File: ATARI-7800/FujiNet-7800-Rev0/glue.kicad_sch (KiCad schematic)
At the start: 10 parts, among them U3 74HCT14, U4 74HCT00, U5 74HCT20, U6 74HCT20

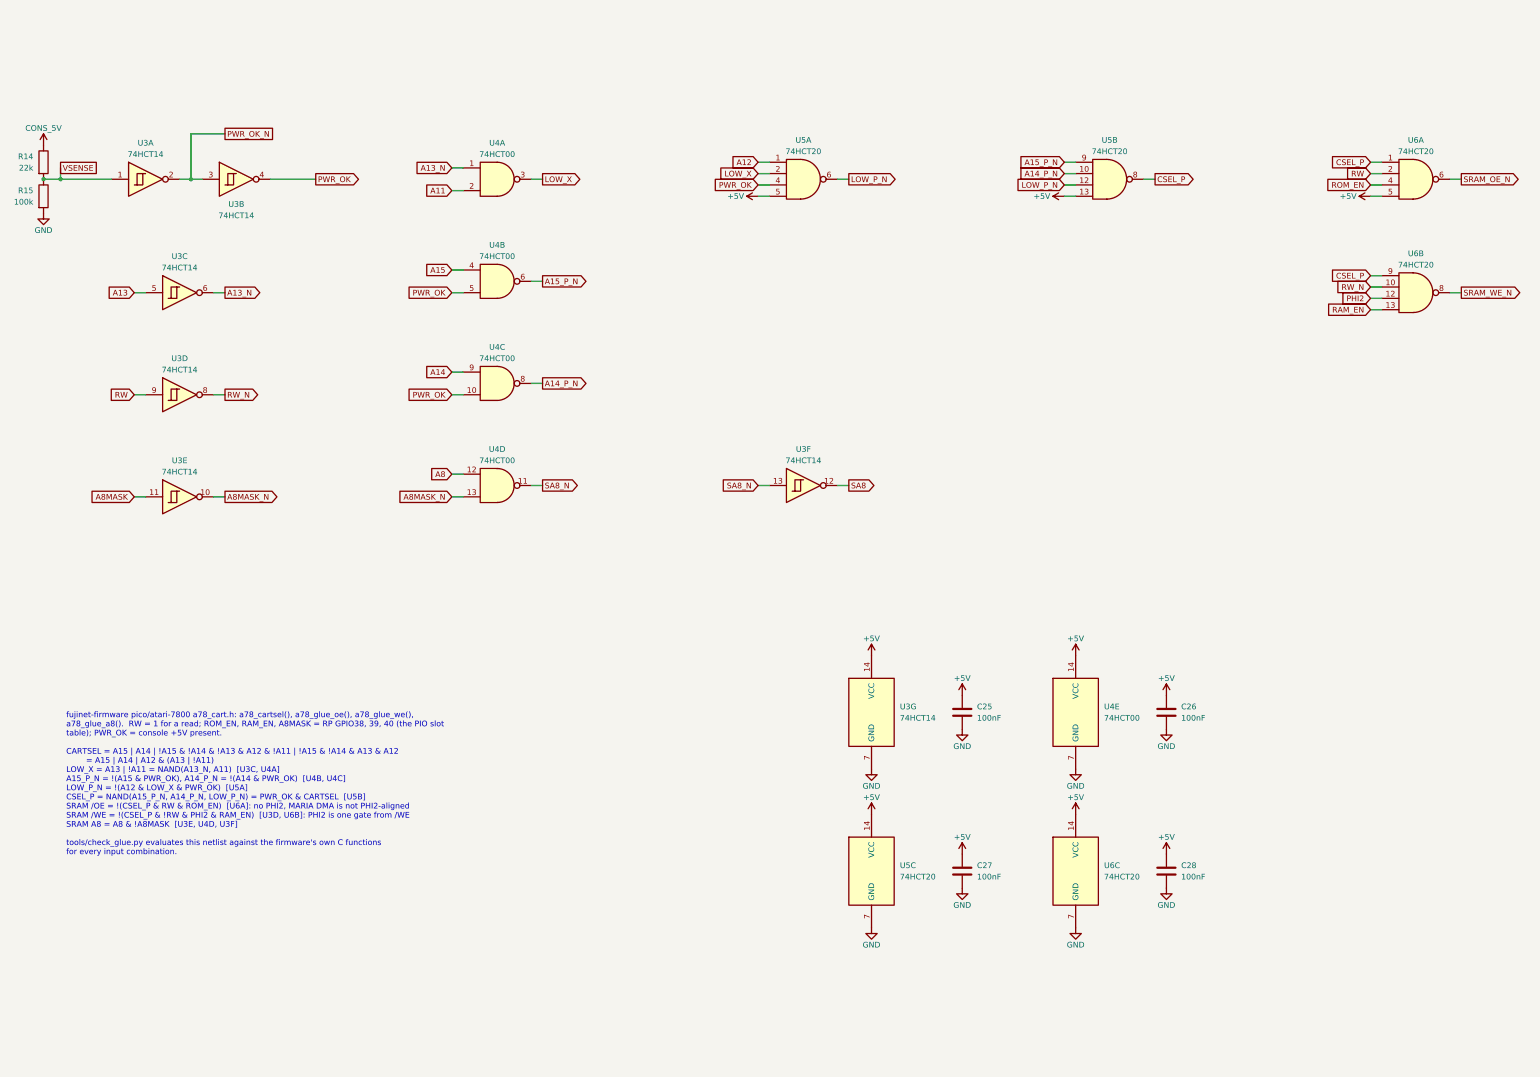
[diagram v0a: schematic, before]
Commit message: ATARI-7800 Rev0: fix the edge, audit the circuit, redraw from the slot, place the board
Edge (board-killer in the schematic-only footprint): the 7800 edge has 18
positions at 2.54 mm with key slots at 3 and 16 for the console's plastic
keys. Pins 1, 2, 15, 16 (and 32, 31, 18, 17) sat one pitch inward, on the
key positions, with no slots and a 42.6 mm tab. tools/edge_geom.py now holds
the geometry (47.0 mm tab, slots centred on +-16.51, 2.4 x 10 mm);
tools/audit/edge_orientation.py checks it against Otaku-flash, tdididit's
boards, the a78-devcart gerbers and this repo's working FujiPlusCart
prototype gerbers (faces and power fingers).

Circuit (console research: Atari C025231 schematic, GCC1702B MARIA spec):
- 4.7k pull-downs on ROM_EN / RAM_EN / A8MASK (RP2350-E9)
- 1k at the /HALT finger (MARIA's HALT is a weak MOS output)
- 10 uF at the console 5V finger; bring-up test pads
- TS-1187A buttons and WS2812C-2020-V1 (the TL3342 and WS2812B-2020
  had 5 in stock at JLC); manufacturer fields for PCBWay
No glue change: R/W is pulled up during MARIA DMA, and the console gates
A15/A14/A12 low while its BIOS is mapped, so CARTSEL never fights it.

Schematic: SMS Rev0's hierarchy (wired root block diagram, hierarchical
labels, netlist parity); sheets in flow order from the slot; the glue
redrawn as a left-to-right gate-depth diagram; references renumbered
from the slot. ERC 0, check_nets 383/383, check_glue 4096/4096.

Board (not yet routed): SMS Rev0's 6-layer pipeline ported. A 72.4 x 115 mm
outline: the stock T-bar width on a 47 x 16.5 mm tab, with the key slots
cut in. Placement variant A (RP over the address fingers, SRAM over the
data fingers): unrouted DRC 0 errors, parity 0, check_vias 0. Shell:
case/FujiNet-7800-Shell.scad. README still describes the old board.

Co-Authored-By: Claude Opus 5.5 <noreply@anthropic.com>
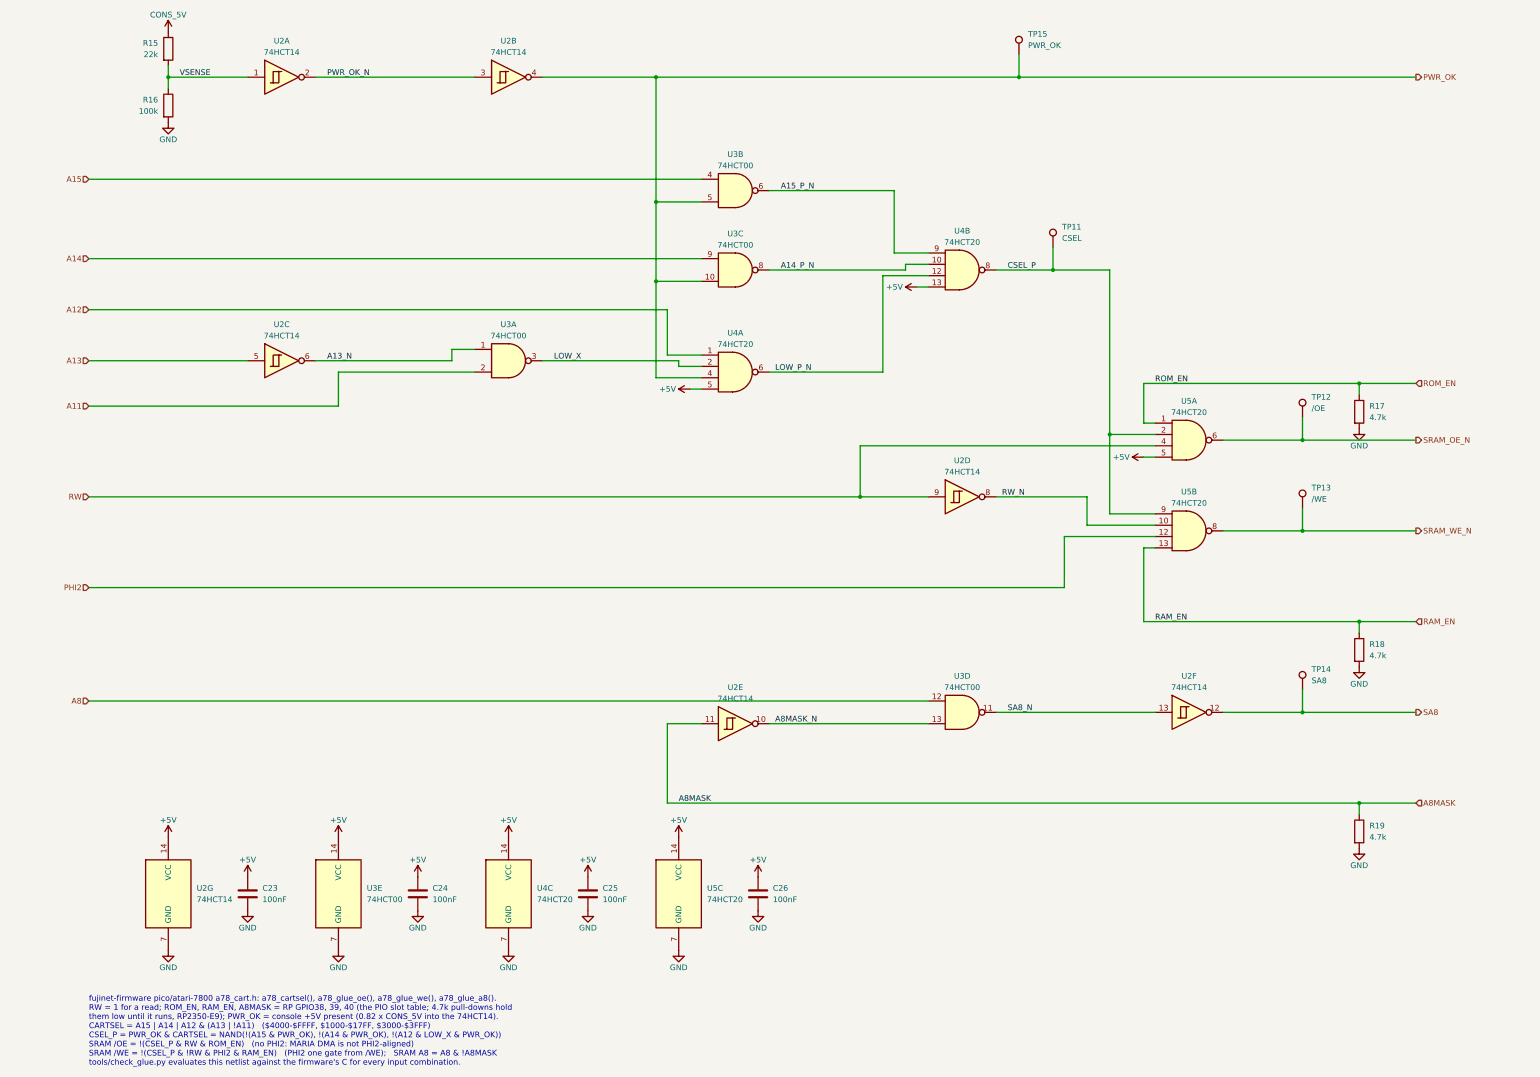
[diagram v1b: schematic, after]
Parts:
- removed C27, C28: 100nF, FujiNet-7800:C_0603_1608Metric, symbol Device:C
- removed R14: 22k, FujiNet-7800:R_0603_1608Metric, symbol Device:R
- removed unit 7 of U3
- removed unit 6 of U3
- removed unit 5 of U4
- removed unit 4 of U4
- removed U6: 74HCT20, FujiNet-7800:SOIC-14_3.9x8.7mm_P1.27mm, symbol 74xx:74LS20
- added C23, C24: 100nF, FujiNet-7800:C_0603_1608Metric, symbol Device:C
- added R16: 100k, FujiNet-7800:R_0603_1608Metric, symbol Device:R
- added R17, R18, R19: 4.7k, FujiNet-7800:R_0603_1608Metric, symbol Device:R
- added TP11: CSEL, FujiNet-7800:TestPoint_Pad_D1.5mm, symbol Connector:TestPoint
- added TP12: /OE, FujiNet-7800:TestPoint_Pad_D1.5mm, symbol Connector:TestPoint
- added TP13: /WE, FujiNet-7800:TestPoint_Pad_D1.5mm, symbol Connector:TestPoint
- added TP14: SA8, FujiNet-7800:TestPoint_Pad_D1.5mm, symbol Connector:TestPoint
- added TP15: PWR_OK, FujiNet-7800:TestPoint_Pad_D1.5mm, symbol Connector:TestPoint
- added U2: 74HCT14, FujiNet-7800:SOIC-14_3.9x8.7mm_P1.27mm, symbol 74xx:74HC14
- R15: value 100k -> 22k; LCSC C25803 -> C31850; MPN 0603WAF1003T5E -> 0603WAF2202T5E
- U3: value 74HCT14 -> 74HCT00; symbol 74xx:74HC14 -> 74xx:74HCT00; LCSC C6769 -> C6764; MPN SN74HCT14DR -> SN74HCT00DR
- U4: value 74HCT00 -> 74HCT20; symbol 74xx:74HCT00 -> 74xx:74LS20; LCSC C6764 -> C2878717; MPN SN74HCT00DR -> CD74HCT20M96
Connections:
- net +5V: now also U3.14 (VCC), U4.13, U4.14 (VCC), U4.5, C23.1, C24.1, U2.14 (VCC); no longer U5.13
- net A11: now also U3.2; no longer U4.2
- net A12: now also U4.1; no longer U5.1
- net A13: now also U2.5; no longer U3.5
- net A13_N: now also U3.1, U2.6; no longer U3.6, U4.1
- net A14: now also U3.9; no longer U4.9
- net A14_P_N: now also U3.8, U4.10; no longer U4.8, U5.10
- net A15: now also U3.4; no longer U4.4
- net A15_P_N: now also U3.6, U4.9; no longer U4.6, U5.9
- net A8: now also U3.12
- net A8MASK: now also R19.1, U2.11; no longer U3.11
- net A8MASK_N: now also U3.13, U2.10; no longer U3.10
- net CONS_5V: now also R15.1
- net CSEL_P: now also U4.8, U5.2, U5.9, TP11.1; no longer U5.8
- net GND: now also U3.7 (GND), U4.7 (GND), C23.2, C24.2, R16.2, R17.2, R18.2, R19.2, U2.7 (GND); no longer R15.2
- net LOW_P_N: now also U4.12, U4.6; no longer U5.12, U5.6
- net LOW_X: now also U3.3, U4.2; no longer U4.3, U5.2
- net PHI2: now also U5.12
- net PWR_OK: now also U3.10, U3.5, U4.4, TP15.1, U2.4; no longer U3.4, U4.10, U4.5, U5.4
- net PWR_OK_N: now also U2.2, U2.3; no longer U3.2, U3.3
- net RAM_EN: now also U5.13, R18.1
- net ROM_EN: now also U5.1, R17.1
- net RW: now also U5.4, U2.9; no longer U3.9
- net RW_N: now also U5.10, U2.8; no longer U3.8
- net SA8: now also TP14.1, U2.12
- net SA8_N: now also U3.11, U2.13
- net SRAM_OE_N: now also U5.6, TP12.1
- net SRAM_WE_N: now also U5.8, TP13.1
- net VSENSE: now also R15.2, R16.1, U2.1; no longer R15.1, U3.1
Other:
- note added: "fujinet-firmware pico/atari-7800 a78_cart.h: a78_cartsel(), a78_glue_oe(), a78_glue_we(), a78_glue_a8(). RW = 1 for a read; ROM_EN, RAM_EN, A8MASK = RP GPIO38, 39, 40 (the PIO slot table; 4.7k pull-downs hold them low until it runs, RP2350-E9); PWR_OK = console +5V present (0.82 x CONS_5V into the 74HCT14). CARTSEL = A15 | A14 | A12 & (A13 | !A11) ($4000-$FFFF, $1000-$17FF, $3000-$3FFF) CSEL_P = 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"
- note removed: "fujinet-firmware pico/atari-7800 a78_cart.h: a78_cartsel(), a78_glue_oe(), a78_glue_we(), a78_glue_a8(). RW = 1 for a read; ROM_EN, RAM_EN, A8MASK = RP GPIO38, 39, 40 (the PIO slot table); PWR_OK = console +5V present. CARTSEL = A15 | A14 | !A15 & !A14 & !A13 & A12 & !A11 | !A15 & !A14 & A13 & A12 = A15 | A14 | A12 & (A13 | !A11) LOW_X = A13 | !A11 = NAND(A13_N, A11) [U3C, U4A] A15_P_N = !(A15 & 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"
- title: FujiNet 7800 Rev0 - 5V glue: CARTSEL, SRAM /OE, /WE, A8, PWR_OK -> FujiNet 7800 Rev0 - 5V glue: CARTSEL, /OE, /WE, A8, PWR_OK
- moved on the sheet: C25, C26, R15, U5A, U5B, U5C
